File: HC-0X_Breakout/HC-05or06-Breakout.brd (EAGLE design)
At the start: 35.2 x 52.1 mm, 23 parts, among them X1 USBSMD

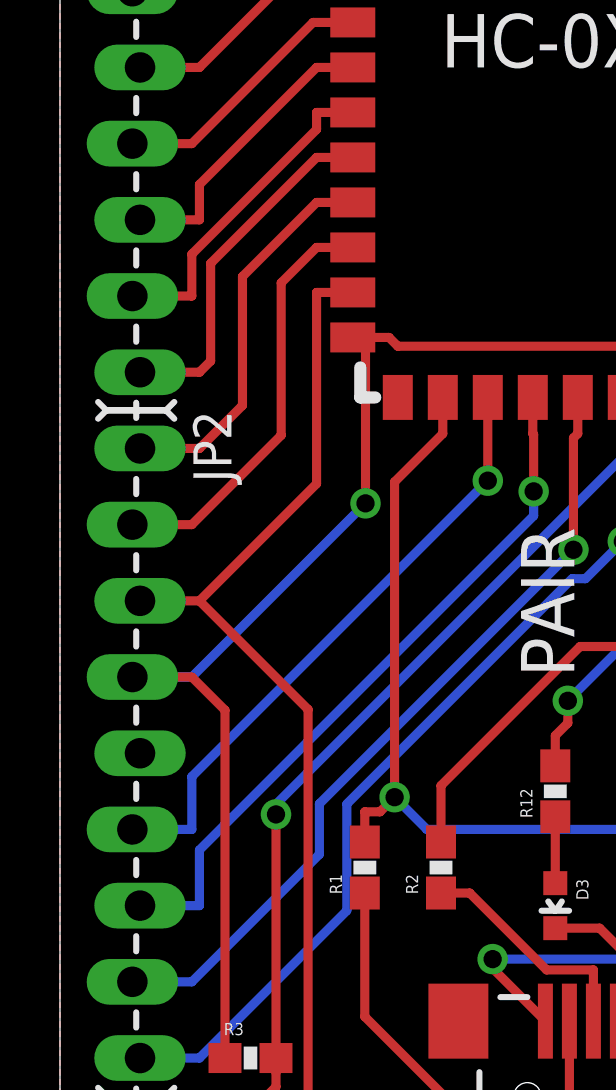
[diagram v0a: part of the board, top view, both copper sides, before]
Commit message: fix silkscreen alignment errors
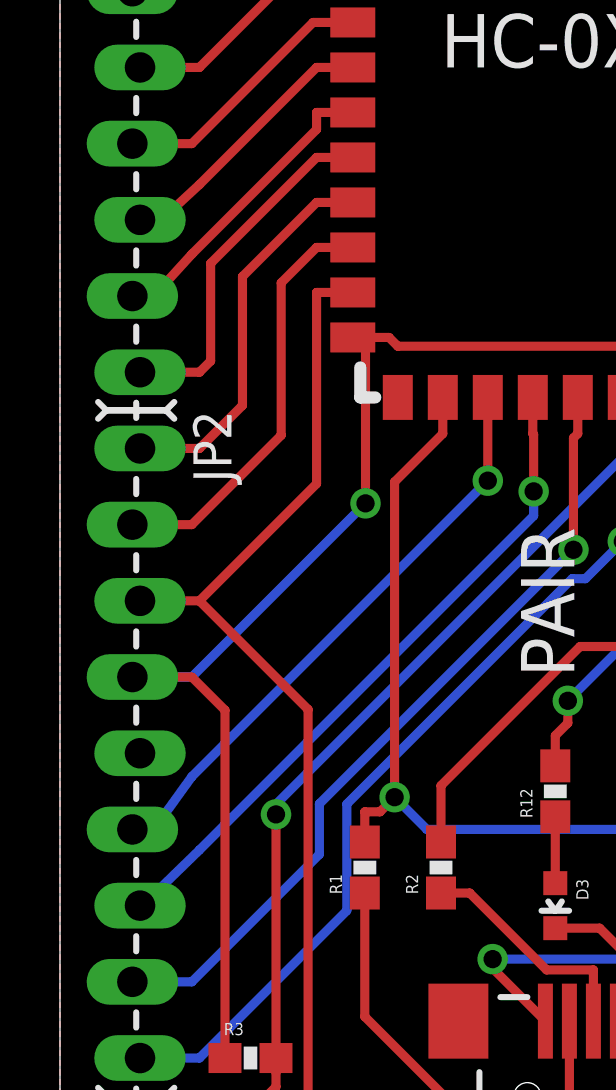
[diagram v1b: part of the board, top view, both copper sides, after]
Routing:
- net MOSI: track 23.5 -> 22.4 mm
- net CS: track 20.5 -> 19.6 mm
- net PCM_SYNC: track 11.0 -> 10.3 mm
- net PCM_IN: track 9.89 -> 9.17 mm
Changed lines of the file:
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@@
 <?xml version="1.0" encoding="utf-8"?>
 <!DOCTYPE eagle SYSTEM "eagle.dtd">
-<eagle version="6.2">
+<eagle version="6.3">
 <drawing>
 <settings>
@@
 <text x="31.115" y="10.795" size="1.27" layer="22" font="vector" rot="MR0" align="top-left">GND</text>
 <text x="31.115" y="8.255" size="1.27" layer="22" font="vector" rot="MR0" align="top-left">VBUS</text>
-<text x="24.13" y="17.145" size="1.778" layer="22" font="vector" rot="MR270" align="bottom-right">HC-0X Breakout Board</text>
-<text x="20.32" y="31.115" size="1.778" layer="22" font="vector" rot="MR270" align="bottom-right">Sterling Peet</text>
-<text x="15.875" y="34.925" size="1.778" layer="22" font="vector" rot="MR270" align="bottom-right">10/3/2012</text>
+<text x="20.955" y="50.8" size="1.778" layer="22" font="vector" rot="MR270" align="top-left">HC-0X Breakout Board</text>
+<text x="16.51" y="50.8" size="1.778" layer="22" font="vector" rot="MR270" align="top-left">Sterling Peet</text>
+<text x="12.065" y="50.8" size="1.778" layer="22" font="vector" rot="MR270" align="top-left">10/3/2012</text>
 </plain>
 <attributes>
@@
 </class>
 </classes>
-<designrules>
+<designrules name="default">
 <description language="de">&lt;b&gt;EAGLE Design Rules&lt;/b&gt;
 &lt;p&gt;
@@
 <contactref element="BT1" pad="P$7"/>
 <contactref element="JP1" pad="7"/>
-<wire x1="4.6483" y1="35.56" x2="4.6483" y2="36.7356" width="0.3048" layer="1"/>
+<wire x1="3.3783" y1="35.56" x2="4.6483" y2="36.7356" width="0.3048" layer="1"/>
 <wire x1="4.6483" y1="36.7356" x2="8.5527" y2="40.64" width="0.3048" layer="1"/>
 <wire x1="9.76" y1="40.64" x2="8.5527" y2="40.64" width="0.3048" layer="1"/>
-<wire x1="2.667" y1="35.56" x2="4.6483" y2="35.56" width="0.3048" layer="1"/>
+<wire x1="2.667" y1="35.56" x2="3.3783" y2="35.56" width="0.3048" layer="1"/>
 </signal>
 <signal name="PCM_SYNC">
@@
 <contactref element="JP1" pad="8"/>
 <wire x1="9.76" y1="39.14" x2="8.5527" y2="39.14" width="0.3048" layer="1"/>
-<wire x1="2.413" y1="33.02" x2="4.3943" y2="33.02" width="0.3048" layer="1"/>
-<wire x1="4.3943" y1="33.02" x2="4.3943" y2="34.415" width="0.3048" layer="1"/>
+<wire x1="2.413" y1="33.02" x2="3.1243" y2="33.02" width="0.3048" layer="1"/>
+<wire x1="3.1243" y1="33.02" x2="4.3943" y2="34.415" width="0.3048" layer="1"/>
 <wire x1="4.3943" y1="34.415" x2="8.5527" y2="38.5734" width="0.3048" layer="1"/>
 <wire x1="8.5527" y1="38.5734" x2="8.5527" y2="39.14" width="0.3048" layer="1"/>
@@
 <contactref element="JP2" pad="6"/>
 <wire x1="14.26" y1="29.64" x2="14.26" y2="26.8656" width="0.3048" layer="1"/>
-<wire x1="4.3943" y1="15.24" x2="4.3943" y2="16.9999" width="0.3048" layer="16"/>
+<wire x1="3.1243" y1="15.24" x2="4.3943" y2="16.9999" width="0.3048" layer="16"/>
 <wire x1="4.3943" y1="16.9999" x2="14.26" y2="26.8656" width="0.3048" layer="16"/>
-<wire x1="2.413" y1="15.24" x2="4.3943" y2="15.24" width="0.3048" layer="16"/>
+<wire x1="2.413" y1="15.24" x2="3.1243" y2="15.24" width="0.3048" layer="16"/>
 <via x="14.26" y="26.8656" extent="1-16" drill="0.6096" diameter="1.016"/>
 </signal>
@@
 <contactref element="BT1" pad="P$17"/>
 <contactref element="JP2" pad="7"/>
-<wire x1="2.667" y1="12.7" x2="4.6483" y2="12.7" width="0.3048" layer="16"/>
+<wire x1="2.667" y1="12.7" x2="2.7433" y2="12.7" width="0.3048" layer="16"/>
 <wire x1="15.76" y1="29.64" x2="15.76" y2="28.4327" width="0.3048" layer="1"/>
 <wire x1="15.7888" y1="26.5083" x2="15.7888" y2="28.4039" width="0.3048" layer="1"/>
 <wire x1="15.7888" y1="28.4039" x2="15.76" y2="28.4327" width="0.3048" layer="1"/>
 <via x="15.7888" y="26.5083" extent="1-16" drill="0.6096" diameter="1.016"/>
-<wire x1="4.6483" y1="12.7" x2="4.6483" y2="14.5544" width="0.3048" layer="16"/>
+<wire x1="2.7433" y1="12.7" x2="4.6483" y2="14.5544" width="0.3048" layer="16"/>
 <wire x1="4.6483" y1="14.5544" x2="15.7887" y2="25.6948" width="0.3048" layer="16"/>
 <wire x1="15.7887" y1="25.6948" x2="15.7887" y2="26.5083" width="0.3048" layer="16"/>
